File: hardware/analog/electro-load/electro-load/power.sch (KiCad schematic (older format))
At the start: 16 parts, among them J2 Jack-DC, U6 NCP1406SNT1G

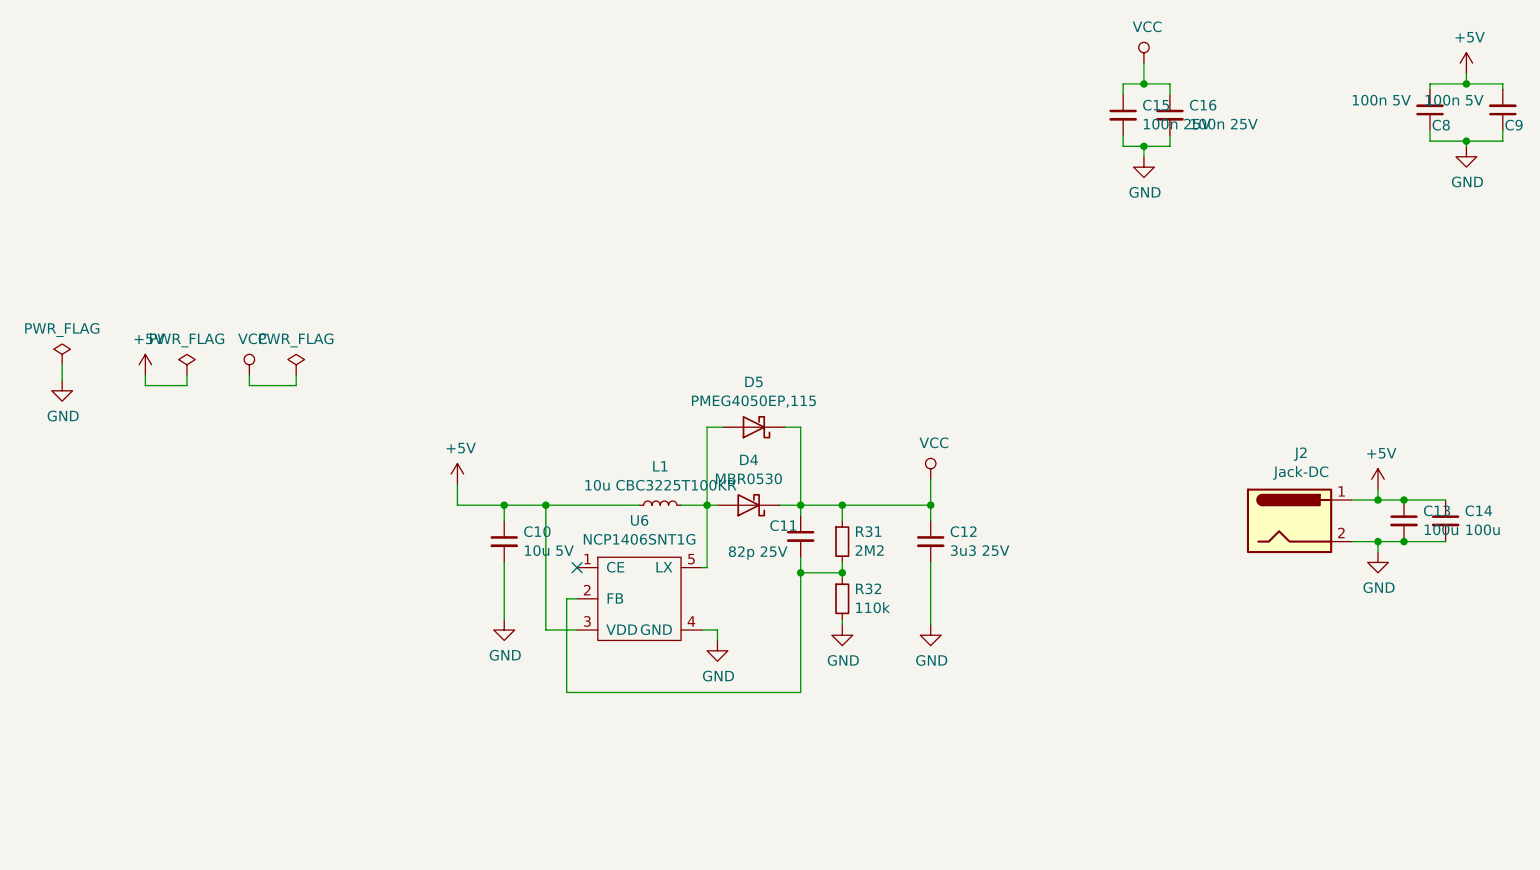
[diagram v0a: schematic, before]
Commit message: Spread schematic out into multiple subsheets. Removed LEDs as pins was needed for 16x2 display
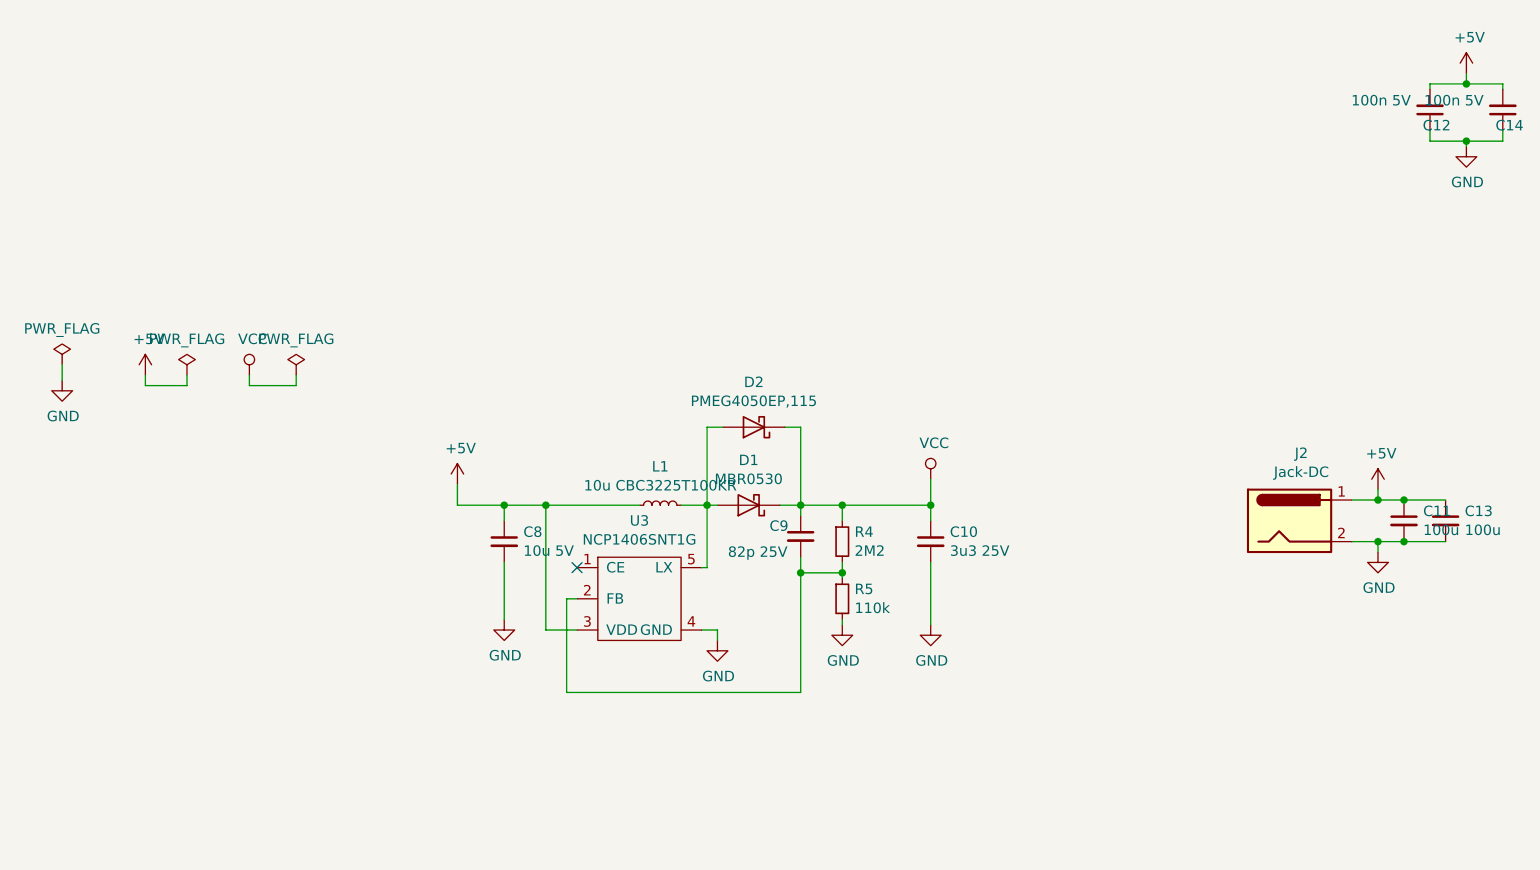
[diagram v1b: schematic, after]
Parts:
- removed C15, C16: 100n 25V, symbol Device:C_Small
- J2: footprint (none) -> Connector_PinHeader_2.54mm:PinHeader_1x02_P2.54mm_Vertical
- renumbered C12 to C10, C13 to C11, C8 to C12, C14 to C13, C9 to C14, C10 to C8, C11 to C9, D4 to D1, D5 to D2, R31 to R4, R32 to R5, U6 to U3
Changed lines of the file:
@@
 $Descr A4 11693 8268
 encoding utf-8
-Sheet 2 2
+Sheet 2 5
 Title ""
 Date ""
@@
 $EndDescr
 $Comp
-L athir:NCP1406SNT1G U6
+L athir:NCP1406SNT1G U3
 U 1 1 5E8D7FC7
 P 4825 3800
-F 0 "U6" H 4925 4125 50  0000 C CNN
+F 0 "U3" H 4925 4125 50  0000 C CNN
 F 1 "NCP1406SNT1G" H 4925 4034 50  0000 C CNN
 F 2 "Package_TO_SOT_SMD:SOT-23-5" H 4825 3800 50  0001 C CNN
@@
 $EndComp
 $Comp
-L Diode:MBR0530 D4
+L Diode:MBR0530 D1
 U 1 1 5E8D8703
 P 5450 3400
-F 0 "D4" H 5450 3184 50  0000 C CNN
+F 0 "D1" H 5450 3184 50  0000 C CNN
 F 1 "MBR0530" H 5450 3275 50  0000 C CNN
 F 2 "Diode_SMD:D_SOD-123" H 5450 3225 50  0001 C CNN
@@
 Connection ~ 4475 3400
 $Comp
-L Device:C_Small C12
+L Device:C_Small C10
 U 1 1 5E8DA00D
 P 6325 3575
-F 0 "C12" H 6417 3621 50  0000 L CNN
+F 0 "C10" H 6417 3621 50  0000 L CNN
 F 1 "3u3 25V" H 6417 3530 50  0000 L CNN
 F 2 "Capacitor_SMD:C_0805_2012Metric" H 6325 3575 50  0001 C CNN
@@
 	6325 3675 6325 3975
 $Comp
-L power:GND #PWR011
+L power:GND #PWR019
 U 1 1 5E8DC920
 P 5300 4050
-F 0 "#PWR011" H 5300 3800 50  0001 C CNN
+F 0 "#PWR019" H 5300 3800 50  0001 C CNN
 F 1 "GND" H 5305 3877 50  0000 C CNN
 F 2 "" H 5300 4050 50  0001 C CNN
@@
 	5300 4050 5300 4000
 $Comp
-L Device:C_Small C11
+L Device:C_Small C9
 U 1 1 5E8DCE2B
 P 5700 3550
-F 0 "C11" H 5550 3600 50  0000 L CNN
+F 0 "C9" H 5550 3600 50  0000 L CNN
 F 1 "82p 25V" H 5350 3475 50  0000 L CNN
 F 2 "Capacitor_SMD:C_0603_1608Metric" H 5700 3550 50  0001 C CNN
@@
 $EndComp
 $Comp
-L Device:R_Small R31
+L Device:R_Small R4
 U 1 1 5E8E2E3F
 P 5900 3575
-F 0 "R31" H 5959 3621 50  0000 L CNN
+F 0 "R4" H 5959 3621 50  0000 L CNN
 F 1 "2M2" H 5959 3530 50  0000 L CNN
 F 2 "Resistor_SMD:R_0603_1608Metric" H 5900 3575 50  0001 C CNN
@@
 $EndComp
 $Comp
-L Device:R_Small R32
+L Device:R_Small R5
 U 1 1 5E8E3F59
 P 5900 3850
-F 0 "R32" H 5959 3896 50  0000 L CNN
+F 0 "R5" H 5959 3896 50  0000 L CNN
 F 1 "110k" H 5959 3805 50  0000 L CNN
 F 2 "Resistor_SMD:R_0603_1608Metric" H 5900 3850 50  0001 C CNN
@@
 Connection ~ 5700 3725
 $Comp
-L Device:C_Small C10
+L Device:C_Small C8
 U 1 1 5E8EC971
 P 4275 3575
-F 0 "C10" H 4367 3621 50  0000 L CNN
+F 0 "C8" H 4367 3621 50  0000 L CNN
 F 1 "10u 5V" H 4367 3530 50  0000 L CNN
 F 2 "Capacitor_SMD:C_0805_2012Metric" H 4275 3575 50  0001 C CNN
@@
 Connection ~ 4275 3400
 $Comp
-L power:GND #PWR010
+L power:GND #PWR018
 U 1 1 5E8ED80A
 P 4275 3950
-F 0 "#PWR010" H 4275 3700 50  0001 C CNN
+F 0 "#PWR018" H 4275 3700 50  0001 C CNN
 F 1 "GND" H 4280 3777 50  0000 C CNN
 F 2 "" H 4275 3950 50  0001 C CNN
@@
 	4050 3400 4275 3400
 $Comp
-L power:+5V #PWR09
+L power:+5V #PWR017
 U 1 1 5E8EE89E
 P 4050 3300
-F 0 "#PWR09" H 4050 3150 50  0001 C CNN
+F 0 "#PWR017" H 4050 3150 50  0001 C CNN
 F 1 "+5V" H 4065 3473 50  0000 C CNN
 F 2 "" H 4050 3300 50  0001 C CNN
@@
 	4050 3300 4050 3400
 $Comp
-L power:VCC #PWR013
+L power:VCC #PWR021
 U 1 1 5E8EF8B6
 P 6325 3275
-F 0 "#PWR013" H 6325 3125 50  0001 C CNN
+F 0 "#PWR021" H 6325 3125 50  0001 C CNN
 F 1 "VCC" H 6342 3448 50  0000 C CNN
 F 2 "" H 6325 3275 50  0001 C CNN
@@
 F 0 "J2" H 8107 3800 50  0000 C CNN
 F 1 "Jack-DC" H 8107 3709 50  0000 C CNN
-F 2 "" H 8100 3435 50  0001 C CNN
+F 2 "Connector_PinHeader_2.54mm:PinHeader_1x02_P2.54mm_Vertical" H 8100 3435 50  0001 C CNN
 F 3 "~" H 8100 3435 50  0001 C CNN
 	1    8050 3475
@@
 P 8475 3625
 AR Path="/5E943757" Ref="#PWR?"  Part="1"
-AR Path="/5E8D69C1/5E943757" Ref="#PWR016"  Part="1"
-F 0 "#PWR016" H 8475 3375 50  0001 C CNN
+AR Path="/5E8D69C1/5E943757" Ref="#PWR024"  Part="1"
+F 0 "#PWR024" H 8475 3375 50  0001 C CNN
 F 1 "GND" H 8480 3452 50  0000 C CNN
 F 2 "" H 8475 3625 50  0001 C CNN
@@
 P 8600 3475
 AR Path="/5E94375D" Ref="C?"  Part="1"
-AR Path="/5E8D69C1/5E94375D" Ref="C13"  Part="1"
-F 0 "C13" H 8692 3521 50  0000 L CNN
+AR Path="/5E8D69C1/5E94375D" Ref="C11"  Part="1"
+F 0 "C11" H 8692 3521 50  0000 L CNN
 F 1 "100u" H 8692 3430 50  0000 L CNN
 F 2 "Capacitor_SMD:CP_Elec_6.3x7.7" H 8600 3475 50  0001 C CNN
@@
 P 8475 3325
 AR Path="/5E943767" Ref="#PWR?"  Part="1"
-AR Path="/5E8D69C1/5E943767" Ref="#PWR015"  Part="1"
-F 0 "#PWR015" H 8475 3175 50  0001 C CNN
+AR Path="/5E8D69C1/5E943767" Ref="#PWR023"  Part="1"
+F 0 "#PWR023" H 8475 3175 50  0001 C CNN
 F 1 "+5V" H 8490 3498 50  0000 C CNN
 F 2 "" H 8475 3325 50  0001 C CNN
@@
 P 8800 3475
 AR Path="/5E94376D" Ref="C?"  Part="1"
-AR Path="/5E8D69C1/5E94376D" Ref="C14"  Part="1"
-F 0 "C14" H 8892 3521 50  0000 L CNN
+AR Path="/5E8D69C1/5E94376D" Ref="C13"  Part="1"
+F 0 "C13" H 8892 3521 50  0000 L CNN
 F 1 "100u" H 8892 3430 50  0000 L CNN
 F 2 "Capacitor_SMD:CP_Elec_6.3x7.7" H 8800 3475 50  0001 C CNN
@@
 P 2150 2800
 AR Path="/5E94377D" Ref="#PWR?"  Part="1"
-AR Path="/5E8D69C1/5E94377D" Ref="#PWR07"  Part="1"
-F 0 "#PWR07" H 2150 2550 50  0001 C CNN
+AR Path="/5E8D69C1/5E94377D" Ref="#PWR014"  Part="1"
+F 0 "#PWR014" H 2150 2550 50  0001 C CNN
 F 1 "GND" H 2155 2627 50  0000 C CNN
 F 2 "" H 2150 2800 50  0001 C CNN
@@
 P 2550 2775
 AR Path="/5E943784" Ref="#PWR?"  Part="1"
-AR Path="/5E8D69C1/5E943784" Ref="#PWR08"  Part="1"
-F 0 "#PWR08" H 2550 2625 50  0001 C CNN
+AR Path="/5E8D69C1/5E943784" Ref="#PWR015"  Part="1"
+F 0 "#PWR015" H 2550 2625 50  0001 C CNN
 F 1 "+5V" H 2565 2948 50  0000 C CNN
 F 2 "" H 2550 2775 50  0001 C CNN
@@
 	5300 4000 5225 4000
 $Comp
-L power:GND #PWR012
+L power:GND #PWR020
 U 1 1 5E95BE14
 P 5900 3975
-F 0 "#PWR012" H 5900 3725 50  0001 C CNN
+F 0 "#PWR020" H 5900 3725 50  0001 C CNN
 F 1 "GND" H 5905 3802 50  0000 C CNN
 F 2 "" H 5900 3975 50  0001 C CNN
@@
 	5900 3950 5900 3975
 $Comp
-L power:GND #PWR014
+L power:GND #PWR022
 U 1 1 5E95CEE6
 P 6325 3975
-F 0 "#PWR014" H 6325 3725 50  0001 C CNN
+F 0 "#PWR022" H 6325 3725 50  0001 C CNN
 F 1 "GND" H 6330 3802 50  0000 C CNN
 F 2 "" H 6325 3975 50  0001 C CNN
@@
 $EndComp
 $Comp
-L power:VCC #PWR0139
+L power:VCC #PWR016
 U 1 1 5E96B3A3
 P 3050 2775
-F 0 "#PWR0139" H 3050 2625 50  0001 C CNN
+F 0 "#PWR016" H 3050 2625 50  0001 C CNN
 F 1 "VCC" H 3067 2948 50  0000 C CNN
 F 2 "" H 3050 2775 50  0001 C CNN
@@
 P 3275 2775
 AR Path="/5E96C8F9" Ref="#FLG?"  Part="1"
-AR Path="/5E8D69C1/5E96C8F9" Ref="#FLG0101"  Part="1"
-F 0 "#FLG0101" H 3275 2850 50  0001 C CNN
+AR Path="/5E8D69C1/5E96C8F9" Ref="#FLG03"  Part="1"
+F 0 "#FLG03" H 3275 2850 50  0001 C CNN
 F 1 "PWR_FLAG" H 3275 2948 50  0000 C CNN
 F 2 "" H 3275 2775 50  0001 C CNN
@@
 	3050 2825 3050 2775
 $Comp
-L power:VCC #PWR0140
-U 1 1 5E98C719
-P 7350 1275
-F 0 "#PWR0140" H 7350 1125 50  0001 C CNN
-F 1 "VCC" H 7367 1448 50  0000 C CNN
-F 2 "" H 7350 1275 50  0001 C CNN
-F 3 "" H 7350 1275 50  0001 C CNN
-	1    7350 1275
-	1    0    0    -1
-$EndComp
-$Comp
-L Device:C_Small C15
-U 1 1 5E98D0D8
-P 7250 1525
-F 0 "C15" H 7342 1571 50  0000 L CNN
-F 1 "100n 25V" H 7342 1480 50  0000 L CNN
-F 2 "" H 7250 1525 50  0001 C CNN
-F 3 "~" H 7250 1525 50  0001 C CNN
-	1    7250 1525
-	1    0    0    -1
-$EndComp
-$Comp
-L Device:C_Small C16
-U 1 1 5E98D8C8
-P 7475 1525
-F 0 "C16" H 7567 1571 50  0000 L CNN
-F 1 "100n 25V" H 7567 1480 50  0000 L CNN
-F 2 "" H 7475 1525 50  0001 C CNN
-F 3 "~" H 7475 1525 50  0001 C CNN
-	1    7475 1525
-	1    0    0    -1
-$EndComp
-Wire Wire Line
-	7475 1425 7475 1375
-$Comp
-L power:GND #PWR0141
-U 1 1 5E98F6ED
-P 7350 1725
-F 0 "#PWR0141" H 7350 1475 50  0001 C CNN
-F 1 "GND" H 7355 1552 50  0000 C CNN
-F 2 "" H 7350 1725 50  0001 C CNN
-F 3 "" H 7350 1725 50  0001 C CNN
-	1    7350 1725
-	1    0    0    -1
-$EndComp
-Wire Wire Line
-	7250 1625 7250 1675
-Wire Wire Line
-	7250 1675 7350 1675
-Wire Wire Line
-	7350 1675 7350 1725
-Wire Wire Line
-	7350 1675 7475 1675
-Wire Wire Line
-	7475 1675 7475 1625
-Connection ~ 7350 1675
-Wire Wire Line
-	7350 1275 7350 1375
-Wire Wire Line
-	7350 1375 7475 1375
-Wire Wire Line
-	7350 1375 7250 1375
-Wire Wire Line
-	7250 1375 7250 1425
-Connection ~ 7350 1375
-$Comp
 L Device:C_Small C?
 U 1 1 5E9EA4CE
 P 8725 1500
 AR Path="/5E9EA4CE" Ref="C?"  Part="1"
-AR Path="/5E8D69C1/5E9EA4CE" Ref="C8"  Part="1"
-F 0 "C8" H 8625 1575 50  0000 L CNN
+AR Path="/5E8D69C1/5E9EA4CE" Ref="C12"  Part="1"
+F 0 "C12" H 8625 1575 50  0000 L CNN
 F 1 "100n 5V" H 8817 1455 50  0000 L CNN
 F 2 "Capacitor_SMD:C_0603_1608Metric" H 8725 1500 50  0001 C CNN
@@
 P 8900 1325
 AR Path="/5E9EA4D6" Ref="#PWR?"  Part="1"
-AR Path="/5E8D69C1/5E9EA4D6" Ref="#PWR0144"  Part="1"
-F 0 "#PWR0144" H 8900 1175 50  0001 C CNN
+AR Path="/5E8D69C1/5E9EA4D6" Ref="#PWR025"  Part="1"
+F 0 "#PWR025" H 8900 1175 50  0001 C CNN
 F 1 "+5V" H 8915 1498 50  0000 C CNN
 F 2 "" H 8900 1325 50  0001 C CNN
@@
 	8900 1325 8900 1375
 $Comp
-L power:GND #PWR0145
+L power:GND #PWR026
 U 1 1 5E9EB603
 P 8900 1675
-F 0 "#PWR0145" H 8900 1425 50  0001 C CNN
+F 0 "#PWR026" H 8900 1425 50  0001 C CNN
 F 1 "GND" H 8905 1502 50  0000 C CNN
 F 2 "" H 8900 1675 50  0001 C CNN
@@
 P 9075 1500
 AR Path="/5E9ED1A5" Ref="C?"  Part="1"
-AR Path="/5E8D69C1/5E9ED1A5" Ref="C9"  Part="1"
-F 0 "C9" H 8975 1575 50  0000 L CNN
+AR Path="/5E8D69C1/5E9ED1A5" Ref="C14"  Part="1"
+F 0 "C14" H 8975 1575 50  0000 L CNN
 F 1 "100n 5V" H 9167 1455 50  0000 L CNN
 F 2 "Capacitor_SMD:C_0603_1608Metric" H 9075 1500 50  0001 C CNN
@@
 Connection ~ 8900 1650
 $Comp
-L Diode:MBR0530 D5
+L Diode:MBR0530 D2
 U 1 1 5EA36565
 P 5475 3025
-F 0 "D5" H 5475 2809 50  0000 C CNN
+F 0 "D2" H 5475 2809 50  0000 C CNN
 F 1 "PMEG4050EP,115" H 5475 2900 50  0000 C CNN
 F 2 "athir:SOD128" H 5475 2850 50  0001 C CNN

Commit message: HW rev 1 of electronic load PCB.
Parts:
- removed C10: 3u3 25V, Capacitor_SMD:C_0805_2012Metric, symbol Device:C_Small
- removed C11, C13: 100u, Capacitor_SMD:CP_Elec_6.3x7.7, symbol Device:C_Small
- removed C12, C14: 100n 5V, Capacitor_SMD:C_0603_1608Metric, symbol Device:C_Small
- removed C8: 10u 5V, Capacitor_SMD:C_0805_2012Metric, symbol Device:C_Small
- removed C9: 82p 25V, Capacitor_SMD:C_0603_1608Metric, symbol Device:C_Small
- removed D1: MBR0530, Diode_SMD:D_SOD-123, symbol Diode:MBR0530
- removed D2: PMEG4050EP,115, athir:SOD128, symbol Diode:MBR0530
- removed L1: 10u CBC3225T100KR, Inductor_SMD:L_1210_3225Metric, symbol Device:L_Small
- removed R4: 2M2, Resistor_SMD:R_0603_1608Metric, symbol Device:R_Small
- removed R5: 110k, Resistor_SMD:R_0603_1608Metric, symbol Device:R_Small
- removed U3: NCP1406SNT1G, Package_TO_SOT_SMD:SOT-23-5, symbol athir:NCP1406SNT1G
- J2: value Jack-DC -> Conn_WallSocket_Earth; footprint Connector_PinHeader_2.54mm:PinHeader_1x02_P2.54mm_Vertical -> athir:230VAC_PLUG
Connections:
- no-connect marks 1 -> 0

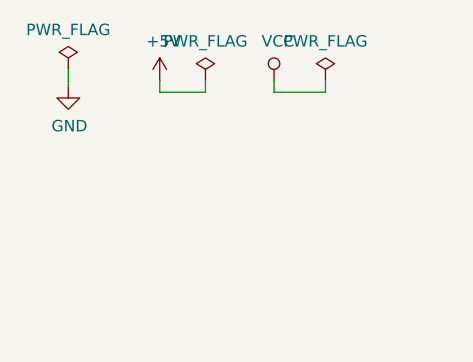
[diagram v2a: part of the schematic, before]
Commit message: Added voltage reference REF5020 datasheet
Started work on HW rev 2 of electro load and 5v-from-mains - rev 1 contained misaligned footprints.
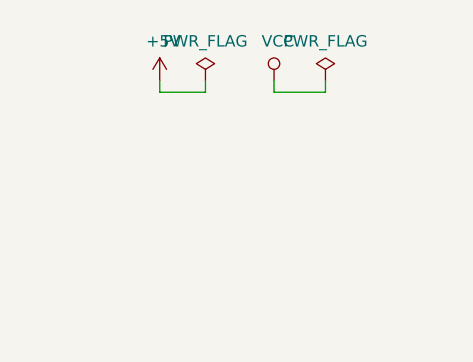
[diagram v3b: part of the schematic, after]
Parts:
- J2: footprint athir:230VAC_PLUG -> athir:Molex-KK-396-5277
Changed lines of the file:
@@
 $EndComp
-$Comp
-L power:GND #PWR?
-U 1 1 5E94377D
-P 2150 2800
-AR Path="/5E94377D" Ref="#PWR?"  Part="1"
-AR Path="/5E8D69C1/5E94377D" Ref="#PWR014"  Part="1"
-F 0 "#PWR014" H 2150 2550 50  0001 C CNN
-F 1 "GND" H 2155 2627 50  0000 C CNN
-F 2 "" H 2150 2800 50  0001 C CNN
-F 3 "" H 2150 2800 50  0001 C CNN
-	1    2150 2800
-	1    0    0    -1
-$EndComp
-Wire Wire Line
-	2150 2800 2150 2725
 $Comp
 L power:+5V #PWR?
@@
 	2750 2825 2750 2775
 $Comp
-L power:PWR_FLAG #FLG?
-U 1 1 5E94378D
-P 2150 2725
-AR Path="/5E94378D" Ref="#FLG?"  Part="1"
-AR Path="/5E8D69C1/5E94378D" Ref="#FLG01"  Part="1"
-F 0 "#FLG01" H 2150 2800 50  0001 C CNN
-F 1 "PWR_FLAG" H 2150 2898 50  0000 C CNN
-F 2 "" H 2150 2725 50  0001 C CNN
-F 3 "~" H 2150 2725 50  0001 C CNN
-	1    2150 2725
-	1    0    0    -1
-$EndComp
-$Comp
-L power:VCC #PWR017
+L power:VCC #PWR016
 U 1 1 5E96B3A3
 P 3050 2775
-F 0 "#PWR017" H 3050 2625 50  0001 C CNN
+F 0 "#PWR016" H 3050 2625 50  0001 C CNN
 F 1 "VCC" H 3067 2948 50  0000 C CNN
 F 2 "" H 3050 2775 50  0001 C CNN
@@
 F 0 "J2" H 2681 5125 50  0000 C CNN
 F 1 "Conn_WallSocket_Earth" H 3350 4800 50  0000 C CNN
-F 2 "athir:230VAC_PLUG" H 2375 4800 50  0001 C CNN
+F 2 "athir:Molex-KK-396-5277" H 2375 4800 50  0001 C CNN
 F 3 "~" H 2375 4800 50  0001 C CNN
 	1    2675 4700
@@
 $EndComp
 $Comp
-L power:+5V #PWR0101
+L power:+5V #PWR017
 U 1 1 5E83C431
 P 3150 4575
-F 0 "#PWR0101" H 3150 4425 50  0001 C CNN
+F 0 "#PWR017" H 3150 4425 50  0001 C CNN
 F 1 "+5V" H 3165 4748 50  0000 C CNN
 F 2 "" H 3150 4575 50  0001 C CNN
@@
 	3150 4800 3150 4850
 $Comp
-L power:GND #PWR0104
+L power:GND #PWR018
 U 1 1 5E83D050
 P 3150 4850
-F 0 "#PWR0104" H 3150 4600 50  0001 C CNN
+F 0 "#PWR018" H 3150 4600 50  0001 C CNN
 F 1 "GND" H 3155 4677 50  0000 C CNN
 F 2 "" H 3150 4850 50  0001 C CNN
